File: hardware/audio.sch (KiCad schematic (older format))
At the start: 24 parts, among them U4 FM8002A, U5 TM8211, U6 FM8002A

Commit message: Dumb leds and stm32 magic
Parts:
- removed FB2, FB3: 100Ohm@100MHz, Inductor_SMD:L_0603_1608Metric, symbol Device:Ferrite_Bead
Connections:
- net 5V: now also C12.1, C14.1, C2.1, C7.1, U4.6 (VDD), U6.6 (VDD)
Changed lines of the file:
@@
 EESchema Schematic File Version 4
-LIBS:cz-badge-hardware-cache
 EELAYER 30 0
 EELAYER END
 $Descr A4 11693 8268
 encoding utf-8
-Sheet 3 3
+Sheet 3 5
 Title ""
 Date ""
@@
 $EndComp
 Connection ~ 6500 2600
-Wire Wire Line
-	6500 2600 6650 2600
 Connection ~ 6500 2300
 Wire Wire Line
@@
 $EndComp
 Connection ~ 6500 3900
-Wire Wire Line
-	6500 3900 6650 3900
 Connection ~ 6500 4200
 Wire Wire Line
@@
 	2400 3550 2200 3550
 Connection ~ 2400 3550
-Wire Wire Line
-	7050 3900 6950 3900
 Text HLabel 7050 3900 1    50   Input ~ 0
 5V
-$Comp
-L Device:Ferrite_Bead FB3
-U 1 1 5DFCD30D
-P 6800 3900
-F 0 "FB3" V 7050 3800 50  0000 L CNN
-F 1 "100Ohm@100MHz" V 6950 3800 50  0000 L CNN
-F 2 "Inductor_SMD:L_0603_1608Metric" V 6730 3900 50  0001 C CNN
-F 3 "~" H 6800 3900 50  0001 C CNN
-	1    6800 3900
-	0    -1   -1   0
-$EndComp
 Text HLabel 7050 2600 3    50   Input ~ 0
 5V
-$Comp
-L Device:Ferrite_Bead FB2
-U 1 1 5DFD1FD3
-P 6800 2600
-F 0 "FB2" V 7050 2500 50  0000 L CNN
-F 1 "100Ohm@100MHz" V 6950 2500 50  0000 L CNN
-F 2 "Inductor_SMD:L_0603_1608Metric" V 6730 2600 50  0001 C CNN
-F 3 "~" H 6800 2600 50  0001 C CNN
-	1    6800 2600
-	0    -1   1    0
-$EndComp
-Wire Wire Line
-	6950 2600 7050 2600
+Wire Wire Line
+	6500 3900 7050 3900
+Wire Wire Line
+	6500 2600 7050 2600
 $EndSCHEMATC

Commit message: Added lcsc partnumbers
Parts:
- C10: LCSC (none) -> C16780
- C11, C14, C2: LCSC (none) -> C14663
- C12, C13, C5, C7: LCSC (none) -> C15849
- R13, R15, R19, R20: LCSC (none) -> C23186
- R16, R18, R21, R22: LCSC (none) -> C25804
- U4, U6: LCSC (none) -> C94625
- U5: LCSC (none) -> C92003
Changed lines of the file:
@@
 F 2 "Package_SO:SSOP-8_3.9x5.05mm_P1.27mm" H 1900 3500 50  0001 C CNN
 F 3 "" H 1900 3500 50  0001 C CNN
+F 4 "C92003" H 1900 3250 50  0001 C CNN "LCSC"
 	1    1900 3250
 	1    0    0    -1
@@
 F 2 "Package_SO:SSOP-8_3.9x5.05mm_P1.27mm" H 4850 2650 50  0001 C CNN
 F 3 "" H 4850 2650 50  0001 C CNN
+F 4 "C94625" H 4850 2400 50  0001 C CNN "LCSC"
 	1    4850 2400
 	1    0    0    -1
@@
 F 2 "Resistor_SMD:R_0603_1608Metric" V 4980 3050 50  0001 C CNN
 F 3 "~" H 5050 3050 50  0001 C CNN
+F 4 "C25804" H 5050 3050 50  0001 C CNN "LCSC"
 	1    5050 3050
 	0    1    1    0
@@
 F 2 "Resistor_SMD:R_0603_1608Metric" V 4680 3050 50  0001 C CNN
 F 3 "~" H 4750 3050 50  0001 C CNN
+F 4 "C25804" H 4750 3050 50  0001 C CNN "LCSC"
 	1    4750 3050
 	0    1    1    0
@@
 F 2 "Capacitor_SMD:C_0603_1608Metric" H 6188 2300 50  0001 C CNN
 F 3 "~" H 6150 2450 50  0001 C CNN
+F 4 "C15849" H 6150 2450 50  0001 C CNN "LCSC"
 	1    6150 2450
 	-1   0    0    1
@@
 F 2 "Capacitor_SMD:C_0603_1608Metric" H 4138 2250 50  0001 C CNN
 F 3 "~" H 4100 2400 50  0001 C CNN
+F 4 "C15849" H 4100 2400 50  0001 C CNN "LCSC"
 	1    4100 2400
 	0    -1   -1   0
@@
 F 2 "Resistor_SMD:R_0603_1608Metric" V 3930 3050 50  0001 C CNN
 F 3 "~" H 4000 3050 50  0001 C CNN
+F 4 "C23186" H 4000 3050 50  0001 C CNN "LCSC"
 	1    4000 3050
 	0    1    1    0
@@
 F 2 "Resistor_SMD:R_0603_1608Metric" V 3630 3050 50  0001 C CNN
 F 3 "~" H 3700 3050 50  0001 C CNN
+F 4 "C23186" H 3700 3050 50  0001 C CNN "LCSC"
 	1    3700 3050
 	0    1    1    0
@@
 F 2 "Package_SO:SSOP-8_3.9x5.05mm_P1.27mm" H 4850 4350 50  0001 C CNN
 F 3 "" H 4850 4350 50  0001 C CNN
+F 4 "C94625" H 4850 4100 50  0001 C CNN "LCSC"
 	1    4850 4100
 	1    0    0    1
@@
 F 2 "Resistor_SMD:R_0603_1608Metric" V 4980 3450 50  0001 C CNN
 F 3 "~" H 5050 3450 50  0001 C CNN
+F 4 "C25804" H 5050 3450 50  0001 C CNN "LCSC"
 	1    5050 3450
 	0    1    -1   0
@@
 F 2 "Resistor_SMD:R_0603_1608Metric" V 4680 3450 50  0001 C CNN
 F 3 "~" H 4750 3450 50  0001 C CNN
+F 4 "C25804" H 4750 3450 50  0001 C CNN "LCSC"
 	1    4750 3450
 	0    1    -1   0
@@
 F 2 "Capacitor_SMD:C_0603_1608Metric" H 6188 3900 50  0001 C CNN
 F 3 "~" H 6150 4050 50  0001 C CNN
+F 4 "C15849" H 6150 4050 50  0001 C CNN "LCSC"
 	1    6150 4050
 	-1   0    0    -1
@@
 F 2 "Capacitor_SMD:C_0603_1608Metric" H 4138 3950 50  0001 C CNN
 F 3 "~" H 4100 4100 50  0001 C CNN
+F 4 "C15849" H 4100 4100 50  0001 C CNN "LCSC"
 	1    4100 4100
 	0    -1   1    0
@@
 F 2 "Resistor_SMD:R_0603_1608Metric" V 3930 3450 50  0001 C CNN
 F 3 "~" H 4000 3450 50  0001 C CNN
+F 4 "C23186" H 4000 3450 50  0001 C CNN "LCSC"
 	1    4000 3450
 	0    1    -1   0
@@
 F 2 "Resistor_SMD:R_0603_1608Metric" V 3630 3450 50  0001 C CNN
 F 3 "~" H 3700 3450 50  0001 C CNN
+F 4 "C23186" H 3700 3450 50  0001 C CNN "LCSC"
 	1    3700 3450
 	0    1    -1   0
@@
 F 2 "Capacitor_SMD:C_0603_1608Metric" H 2038 3700 50  0001 C CNN
 F 3 "~" H 2000 3850 50  0001 C CNN
+F 4 "C14663" H 2000 3850 50  0001 C CNN "LCSC"
 	1    2000 3850
 	1    0    0    -1
@@
 F 2 "Capacitor_SMD:C_0805_2012Metric" H 1838 3700 50  0001 C CNN
 F 3 "~" H 1800 3850 50  0001 C CNN
+F 4 "C16780" H 1800 3850 50  0001 C CNN "LCSC"
 	1    1800 3850
 	1    0    0    -1
@@
 F 2 "Capacitor_SMD:C_0603_1608Metric" H 6538 2300 50  0001 C CNN
 F 3 "~" H 6500 2450 50  0001 C CNN
+F 4 "C14663" H 6500 2450 50  0001 C CNN "LCSC"
 	1    6500 2450
 	-1   0    0    1
@@
 F 2 "Capacitor_SMD:C_0603_1608Metric" H 6538 3900 50  0001 C CNN
 F 3 "~" H 6500 4050 50  0001 C CNN
+F 4 "C14663" H 6500 4050 50  0001 C CNN "LCSC"
 	1    6500 4050
 	-1   0    0    -1

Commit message: Wrover fp
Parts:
- added TP1, TP3, TP4: TestPoint, TestPoint:TestPoint_Pad_D1.5mm, symbol Connector:TestPoint
- C8, C9: LCSC (none) -> C1623
- FB1: footprint Inductor_SMD:L_0603_1608Metric -> Inductor_SMD:L_0805_2012Metric; LCSC (none) -> C1017
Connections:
- net at C10.1, C11.1, FB1.1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: now also TP1.1
- net at C9.2, U5.6 (LCH): now also TP4.1
- net at C8.2, U5.8 (RCH): now also TP3.1
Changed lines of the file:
@@
 F 2 "Capacitor_SMD:C_0603_1608Metric" H 3438 2900 50  0001 C CNN
 F 3 "~" H 3400 3050 50  0001 C CNN
+F 4 "C1623" H 3400 3050 50  0001 C CNN "LCSC"
 	1    3400 3050
 	0    1    1    0
@@
 F 2 "Capacitor_SMD:C_0603_1608Metric" H 3438 3300 50  0001 C CNN
 F 3 "~" H 3400 3450 50  0001 C CNN
+F 4 "C1623" H 3400 3450 50  0001 C CNN "LCSC"
 	1    3400 3450
 	0    1    -1   0
@@
 F 0 "FB1" H 2537 3746 50  0000 L CNN
 F 1 "100Ohm@100MHz" H 2537 3655 50  0000 L CNN
-F 2 "Inductor_SMD:L_0603_1608Metric" V 2330 3700 50  0001 C CNN
+F 2 "Inductor_SMD:L_0805_2012Metric" V 2330 3700 50  0001 C CNN
 F 3 "~" H 2400 3700 50  0001 C CNN
+F 4 "C1017" H 2400 3700 50  0001 C CNN "LCSC"
 	1    2400 3700
 	1    0    0    -1
@@
 Wire Wire Line
 	6500 2600 7050 2600
+$Comp
+L Connector:TestPoint TP1
+U 1 1 5E48F618
+P 2450 3450
+F 0 "TP1" V 2404 3638 50  0000 L CNN
+F 1 "TestPoint" V 2495 3638 50  0000 L CNN
+F 2 "TestPoint:TestPoint_Pad_D1.5mm" H 2650 3450 50  0001 C CNN
+F 3 "~" H 2650 3450 50  0001 C CNN
+	1    2450 3450
+	0    1    1    0
+$EndComp
+Wire Wire Line
+	2450 3450 2400 3450
+Connection ~ 2400 3450
+$Comp
+L Connector:TestPoint TP3
+U 1 1 5E4920BF
+P 3050 3000
+F 0 "TP3" H 3108 3118 50  0000 L CNN
+F 1 "TestPoint" H 3108 3027 50  0000 L CNN
+F 2 "TestPoint:TestPoint_Pad_D1.5mm" H 3250 3000 50  0001 C CNN
+F 3 "~" H 3250 3000 50  0001 C CNN
+	1    3050 3000
+	1    0    0    -1
+$EndComp
+Wire Wire Line
+	3050 3000 3050 3050
+Connection ~ 3050 3050
+$Comp
+L Connector:TestPoint TP4
+U 1 1 5E493FE0
+P 3050 3500
+F 0 "TP4" H 2992 3526 50  0000 R CNN
+F 1 "TestPoint" H 2992 3617 50  0000 R CNN
+F 2 "TestPoint:TestPoint_Pad_D1.5mm" H 3250 3500 50  0001 C CNN
+F 3 "~" H 3250 3500 50  0001 C CNN
+	1    3050 3500
+	-1   0    0    1
+$EndComp
+Wire Wire Line
+	3050 3500 3050 3450
+Connection ~ 3050 3450
 $EndSCHEMATC

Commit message: Rev5 schematic changes and pcb cleanup
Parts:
- removed FB1: 100Ohm@100MHz, Inductor_SMD:L_0805_2012Metric, symbol Device:Ferrite_Bead
- added C? (x2): 1uF, Capacitor_SMD:C_0603_1608Metric, symbol Device:C
- added R28, R?: 10, Resistor_SMD:R_0603_1608Metric, symbol Device:R
- added U?: HX9193-33GB, Package_TO_SOT_SMD:SOT-23-5, symbol Regulator_Linear:MIC5504-3.3YM5
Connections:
- net GND: now also C?.1, C?.2, U?.2 (GND)
- net at C10.1, C11.1, TP1.1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: now also R28.2, R?.2
- new net: C?.1, R?.1, U?.5 (VOUT)
- new net 3V3: R28.1
- new net VCC: C?.2, U?.1 (VIN), U?.3 (EN)
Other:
- note added: "3V power"
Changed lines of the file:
@@
 	1300 3450 1400 3450
-Wire Wire Line
-	2400 3550 2400 3450
 Wire Wire Line
 	2400 3450 2350 3450
@@
 Wire Wire Line
 	2400 3950 2400 3850
-Text HLabel 2400 3950 2    50   Input ~ 0
-5V
 $Comp
 L Device:C C11
@@
 	1    0    0    -1
 $EndComp
-$Comp
-L Device:Ferrite_Bead FB1
-U 1 1 5DF0F498
-P 2400 3700
-F 0 "FB1" H 2537 3746 50  0000 L CNN
-F 1 "100Ohm@100MHz" H 2537 3655 50  0000 L CNN
-F 2 "Inductor_SMD:L_0805_2012Metric" V 2330 3700 50  0001 C CNN
-F 3 "~" H 2400 3700 50  0001 C CNN
-F 4 "C1017" H 2400 3700 50  0001 C CNN "LCSC"
-	1    2400 3700
-	1    0    0    -1
-$EndComp
 Wire Wire Line
 	6150 2300 6500 2300
@@
 Wire Wire Line
 	2400 3550 2200 3550
-Connection ~ 2400 3550
 Text HLabel 7050 3900 1    50   Input ~ 0
 5V
@@
 	3050 3500 3050 3450
 Connection ~ 3050 3450
+Text GLabel 2400 3950 3    50   UnSpc ~ 0
+3V3
+$Comp
+L Device:R R28
+U 1 1 5EE31536
+P 2400 3700
+F 0 "R28" V 2193 3700 50  0000 C CNN
+F 1 "10" V 2284 3700 50  0000 C CNN
+F 2 "Resistor_SMD:R_0603_1608Metric" V 2330 3700 50  0001 C CNN
+F 3 "~" H 2400 3700 50  0001 C CNN
+F 4 "" H 2400 3700 50  0001 C CNN "LCSC"
+	1    2400 3700
+	1    0    0    1
+$EndComp
+Connection ~ 2400 3550
+Wire Wire Line
+	2400 3450 2400 3550
+Text GLabel 1000 4600 0    50   UnSpc ~ 0
+VCC
+Wire Wire Line
+	1000 4600 1050 4600
+Text GLabel 1500 5100 0    50   UnSpc ~ 0
+GND
+Text Notes 1300 4250 0    98   ~ 0
+3V power
+$Comp
+L Device:C C?
+U 1 1 5EE458A4
+P 1100 4400
+AR Path="/5EE458A4" Ref="C?"  Part="1"
+AR Path="/5E4377A8/5EE458A4" Ref="C?"  Part="1"
+AR Path="/5E464BBE/5EE458A4" Ref="C?"  Part="1"
+F 0 "C?" V 848 4400 50  0000 C CNN
+F 1 "1uF" V 939 4400 50  0000 C CNN
+F 2 "Capacitor_SMD:C_0603_1608Metric" H 1138 4250 50  0001 C CNN
+F 3 "~" H 1100 4400 50  0001 C CNN
+F 4 "C15849" H 1100 4400 50  0001 C CNN "LCSC"
+	1    1100 4400
+	0    -1   1    0
+$EndComp
+$Comp
+L Device:C C?
+U 1 1 5EE458AB
+P 2200 4400
+AR Path="/5EE458AB" Ref="C?"  Part="1"
+AR Path="/5E4377A8/5EE458AB" Ref="C?"  Part="1"
+AR Path="/5E464BBE/5EE458AB" Ref="C?"  Part="1"
+F 0 "C?" V 1948 4400 50  0000 C CNN
+F 1 "1uF" V 2039 4400 50  0000 C CNN
+F 2 "Capacitor_SMD:C_0603_1608Metric" H 2238 4250 50  0001 C CNN
+F 3 "~" H 2200 4400 50  0001 C CNN
+F 4 "C15849" H 2200 4400 50  0001 C CNN "LCSC"
+	1    2200 4400
+	0    -1   1    0
+$EndComp
+Text GLabel 950  4400 0    50   UnSpc ~ 0
+GND
+Wire Wire Line
+	1250 4400 1250 4500
+Wire Wire Line
+	1250 4500 1150 4500
+Wire Wire Line
+	1150 4500 1150 4550
+Wire Wire Line
+	1150 4550 1050 4550
+Wire Wire Line
+	1050 4550 1050 4600
+Connection ~ 1050 4600
+Wire Wire Line
+	2050 4400 2050 4500
+Wire Wire Line
+	2050 4500 2150 4500
+Wire Wire Line
+	2150 4500 2150 4550
+Wire Wire Line
+	2150 4550 2250 4550
+Wire Wire Line
+	2250 4550 2250 4600
+Connection ~ 2250 4600
+Text GLabel 2350 4400 2    50   UnSpc ~ 0
+GND
+$Comp
+L Regulator_Linear:MIC5504-3.3YM5 U?
+U 1 1 5EE458C0
+P 1650 4700
+F 0 "U?" H 1650 5067 50  0000 C CNN
+F 1 " HX9193-33GB" H 1650 4976 50  0000 C CNN
+F 2 "Package_TO_SOT_SMD:SOT-23-5" H 1650 4300 50  0001 C CNN
+F 3 "" H 1400 4950 50  0001 C CNN
+F 4 "C296123" H 1650 4700 50  0001 C CNN "LCSC"
+	1    1650 4700
+	1    0    0    -1
+$EndComp
+Wire Wire Line
+	2050 4600 2250 4600
+Wire Wire Line
+	1050 4600 1150 4600
+Wire Wire Line
+	1650 5100 1650 5000
+Wire Wire Line
+	1500 5100 1650 5100
+Wire Wire Line
+	1250 4800 1150 4800
+Wire Wire Line
+	1150 4800 1150 4600
+Connection ~ 1150 4600
+Wire Wire Line
+	1150 4600 1250 4600
+$Comp
+L Device:R R?
+U 1 1 5EE48409
+P 2550 3700
+F 0 "R?" V 2343 3700 50  0000 C CNN
+F 1 "10" V 2434 3700 50  0000 C CNN
+F 2 "Resistor_SMD:R_0603_1608Metric" V 2480 3700 50  0001 C CNN
+F 3 "~" H 2550 3700 50  0001 C CNN
+F 4 "" H 2550 3700 50  0001 C CNN "LCSC"
+	1    2550 3700
+	1    0    0    1
+$EndComp
+Wire Wire Line
+	2400 3550 2550 3550
+Wire Wire Line
+	2550 3850 2550 4600
+Wire Wire Line
+	2250 4600 2550 4600
 $EndSCHEMATC

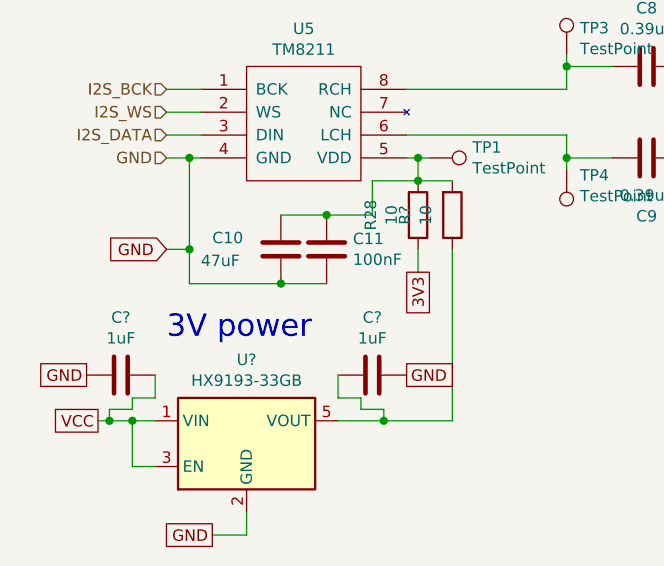
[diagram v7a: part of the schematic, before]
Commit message: Major routing of the led matrix done
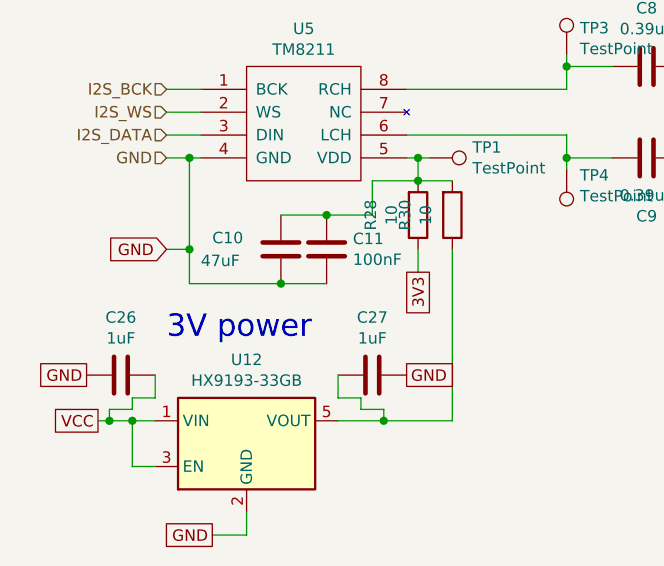
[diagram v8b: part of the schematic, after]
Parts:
- gave numbers to parts that had none: 4
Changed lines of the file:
@@
 AR Path="/5E4377A8/5EE458A4" Ref="C?"  Part="1"
 AR Path="/5E464BBE/5EE458A4" Ref="C?"  Part="1"
-F 0 "C?" V 848 4400 50  0000 C CNN
+AR Path="/5DD7D9A9/5EE458A4" Ref="C26"  Part="1"
+F 0 "C26" V 848 4400 50  0000 C CNN
 F 1 "1uF" V 939 4400 50  0000 C CNN
 F 2 "Capacitor_SMD:C_0603_1608Metric" H 1138 4250 50  0001 C CNN
@@
 AR Path="/5E4377A8/5EE458AB" Ref="C?"  Part="1"
 AR Path="/5E464BBE/5EE458AB" Ref="C?"  Part="1"
-F 0 "C?" V 1948 4400 50  0000 C CNN
+AR Path="/5DD7D9A9/5EE458AB" Ref="C27"  Part="1"
+F 0 "C27" V 1948 4400 50  0000 C CNN
 F 1 "1uF" V 2039 4400 50  0000 C CNN
 F 2 "Capacitor_SMD:C_0603_1608Metric" H 2238 4250 50  0001 C CNN
@@
 U 1 1 5EE458C0
 P 1650 4700
-F 0 "U?" H 1650 5067 50  0000 C CNN
+AR Path="/5E464BBE/5EE458C0" Ref="U?"  Part="1"
+AR Path="/5DD7D9A9/5EE458C0" Ref="U12"  Part="1"
+F 0 "U12" H 1650 5067 50  0000 C CNN
 F 1 " HX9193-33GB" H 1650 4976 50  0000 C CNN
 F 2 "Package_TO_SOT_SMD:SOT-23-5" H 1650 4300 50  0001 C CNN
@@
 	1150 4600 1250 4600
 $Comp
-L Device:R R?
+L Device:R R30
 U 1 1 5EE48409
 P 2550 3700
-F 0 "R?" V 2343 3700 50  0000 C CNN
+F 0 "R30" V 2343 3700 50  0000 C CNN
 F 1 "10" V 2434 3700 50  0000 C CNN
 F 2 "Resistor_SMD:R_0603_1608Metric" V 2480 3700 50  0001 C CNN
